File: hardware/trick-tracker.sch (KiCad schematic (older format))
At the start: 47 parts, among them J1 USB4105-GF-A, J2 S2B-PH-K, J3 QWiiC, U1 MS88SF2, U2 DPS368XTSA1, U3 LSM9DS1, U4 MCP73831-2-OT, U5 MIC5504-3.3YM5

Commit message: Add Micro SD-Card holder
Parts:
- removed LED1: APHF1608LSEEQBDZGKC, APHF1608LSEEQBDZGKC:APHF1608LSEEQBDZGKC, symbol APHF1608LSEEQBDZGKC:APHF1608LSEEQBDZGKC
- removed R8: 2k2, Resistor_SMD:R_0603_1608Metric, symbol Device:R_Small
- removed R9: 390R, Resistor_SMD:R_0603_1608Metric, symbol Device:R_Small
- added D4: GREEN, LED_SMD:LED_0603_1608Metric, symbol Device:LED_Small
- added H3, H4: MountingHole, MountingHole:MountingHole_2.5mm, symbol Mechanical:MountingHole
- added J4: MEM2051-00-195-00-A, MEM2051-00-195-00-A:GCT_MEM2051-00-195-00-A, symbol MEM2051-00-195-00-A:MEM2051-00-195-00-A
- R7: value 1k2 -> 470
- U4: value MCP73831-2-OT -> MCP73831/OT
- gave numbers to parts that had none: 3
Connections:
- net labels added: CS, MISO, MOSI, SCK, SD_DETECT
- net labels removed: CC1, CC2, LED_BLUE, LED_GREEN, LED_RED, NFC1
- wire segments 183 -> 185
- no-connect marks 8 -> 9
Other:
- moved on the sheet: C10, C11, C12, C5, C6, C7, C8, C9, D1, H1, H2, J1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

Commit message: Moved components
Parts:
- added D5: DSS13UTR, Diode_SMD:D_SOD-123F, symbol Device:D_Schottky
- D1: value MBR120 -> DSS13UTR; footprint Diode_SMD:D_0603_1608Metric -> Diode_SMD:D_SOD-123F
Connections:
- net VBUS: now also D5.2 (A); no longer C1.1, D1.1 (K), S3.3 (COM), U5.1 (VIN)
- new net VIN: C1.1, D1.1 (K), D5.1 (K), S3.3 (COM), U5.1 (VIN)
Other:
- moved on the sheet: D1
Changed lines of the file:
@@
 Text Label 7850 3700 0    50   ~ 0
 VBUS
-Text Label 7850 3950 0    50   ~ 0
+Text Label 7850 4050 0    50   ~ 0
 VBAT
 Wire Wire Line
@@
 	9100 3900 9100 3950
 Wire Wire Line
-	7850 3700 8550 3700
-Wire Wire Line
 	9100 3700 9400 3700
-Wire Wire Line
-	8550 3700 8550 3950
-Connection ~ 8550 3700
 Wire Wire Line
 	9700 4150 9400 4150
@@
 L Device:D_Schottky D1
 U 1 1 60B07CC4
-P 8300 3950
-F 0 "D1" H 8300 3733 50  0000 C CNN
-F 1 "MBR120" H 8300 3824 50  0000 C CNN
-F 2 "Diode_SMD:D_0603_1608Metric" H 8300 3950 50  0001 C CNN
-F 3 "~" H 8300 3950 50  0001 C CNN
-	1    8300 3950
+P 8300 4050
+F 0 "D1" H 8300 3833 50  0000 C CNN
+F 1 "DSS13UTR" H 8300 3924 50  0000 C CNN
+F 2 "Diode_SMD:D_SOD-123F" H 8300 4050 50  0001 C CNN
+F 3 "~" H 8300 4050 50  0001 C CNN
+	1    8300 4050
 	-1   0    0    1
 $EndComp
 Wire Wire Line
-	8450 3950 8550 3950
-Wire Wire Line
-	8150 3950 7850 3950
+	8450 4050 8550 4050
+Wire Wire Line
+	8150 4050 7850 4050
 $Comp
 L Connector:Conn_01x04_Male J3
@@
 Wire Wire Line
 	2750 2650 2250 2650
-Wire Wire Line
-	8550 3700 9100 3700
 $Comp
 L MEM2051-00-195-00-A:MEM2051-00-195-00-A J4
@@
 Wire Notes Line
 	500  5150 7350 5150
+$Comp
+L Device:D_Schottky D5
+U 1 1 60D58FCE
+P 8300 3700
+F 0 "D5" H 8300 3483 50  0000 C CNN
+F 1 "DSS13UTR" H 8300 3574 50  0000 C CNN
+F 2 "Diode_SMD:D_SOD-123F" H 8300 3700 50  0001 C CNN
+F 3 "~" H 8300 3700 50  0001 C CNN
+	1    8300 3700
+	-1   0    0    1
+$EndComp
+Wire Wire Line
+	7850 3700 8150 3700
+Wire Wire Line
+	8450 3700 8550 3700
+Wire Wire Line
+	8550 3700 8550 4050
+Connection ~ 8550 3700
+Wire Wire Line
+	8550 3700 9100 3700
 $EndSCHEMATC

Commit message: Changed LED resistor value to 1k
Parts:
- R5, R6: value 470 -> 1k
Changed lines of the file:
@@
 P 10500 2550
 F 0 "R5" V 10304 2550 50  0000 C CNN
-F 1 "470" V 10395 2550 50  0000 C CNN
+F 1 "1k" V 10395 2550 50  0000 C CNN
 F 2 "Resistor_SMD:R_0603_1608Metric" H 10500 2550 50  0001 C CNN
 F 3 "~" H 10500 2550 50  0001 C CNN
@@
 P 10500 2900
 F 0 "R6" V 10304 2900 50  0000 C CNN
-F 1 "470" V 10395 2900 50  0000 C CNN
+F 1 "1k" V 10395 2900 50  0000 C CNN
 F 2 "Resistor_SMD:R_0603_1608Metric" H 10500 2900 50  0001 C CNN
 F 3 "~" H 10500 2900 50  0001 C CNN

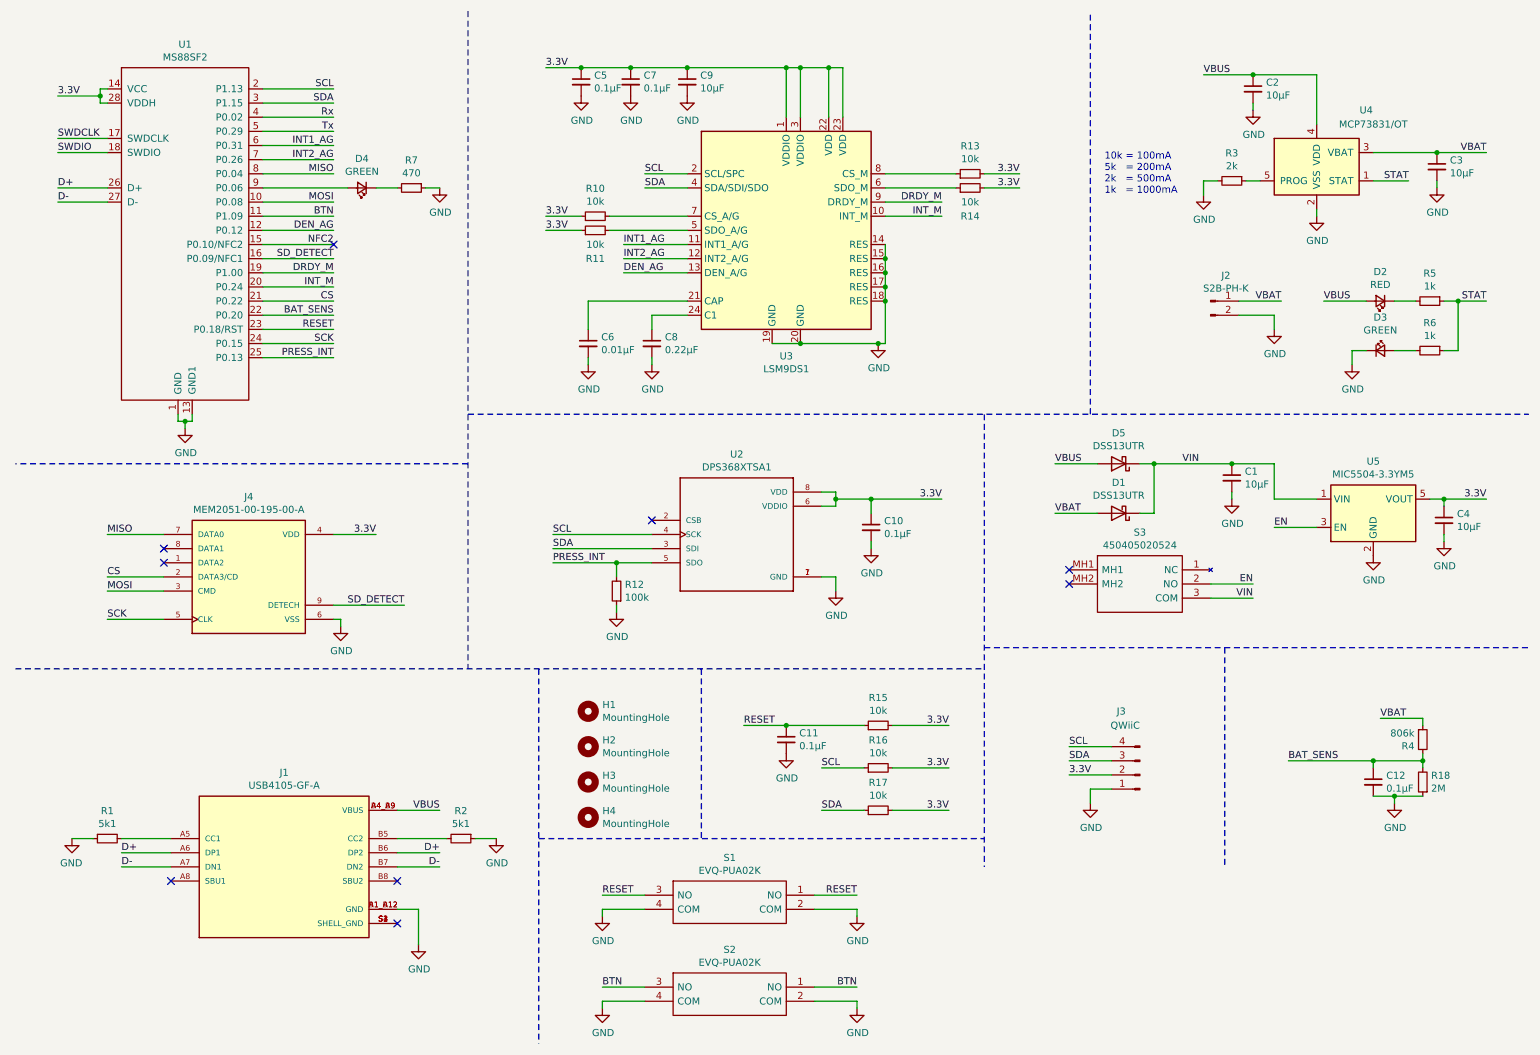
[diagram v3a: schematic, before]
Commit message: Add Labels to schematic
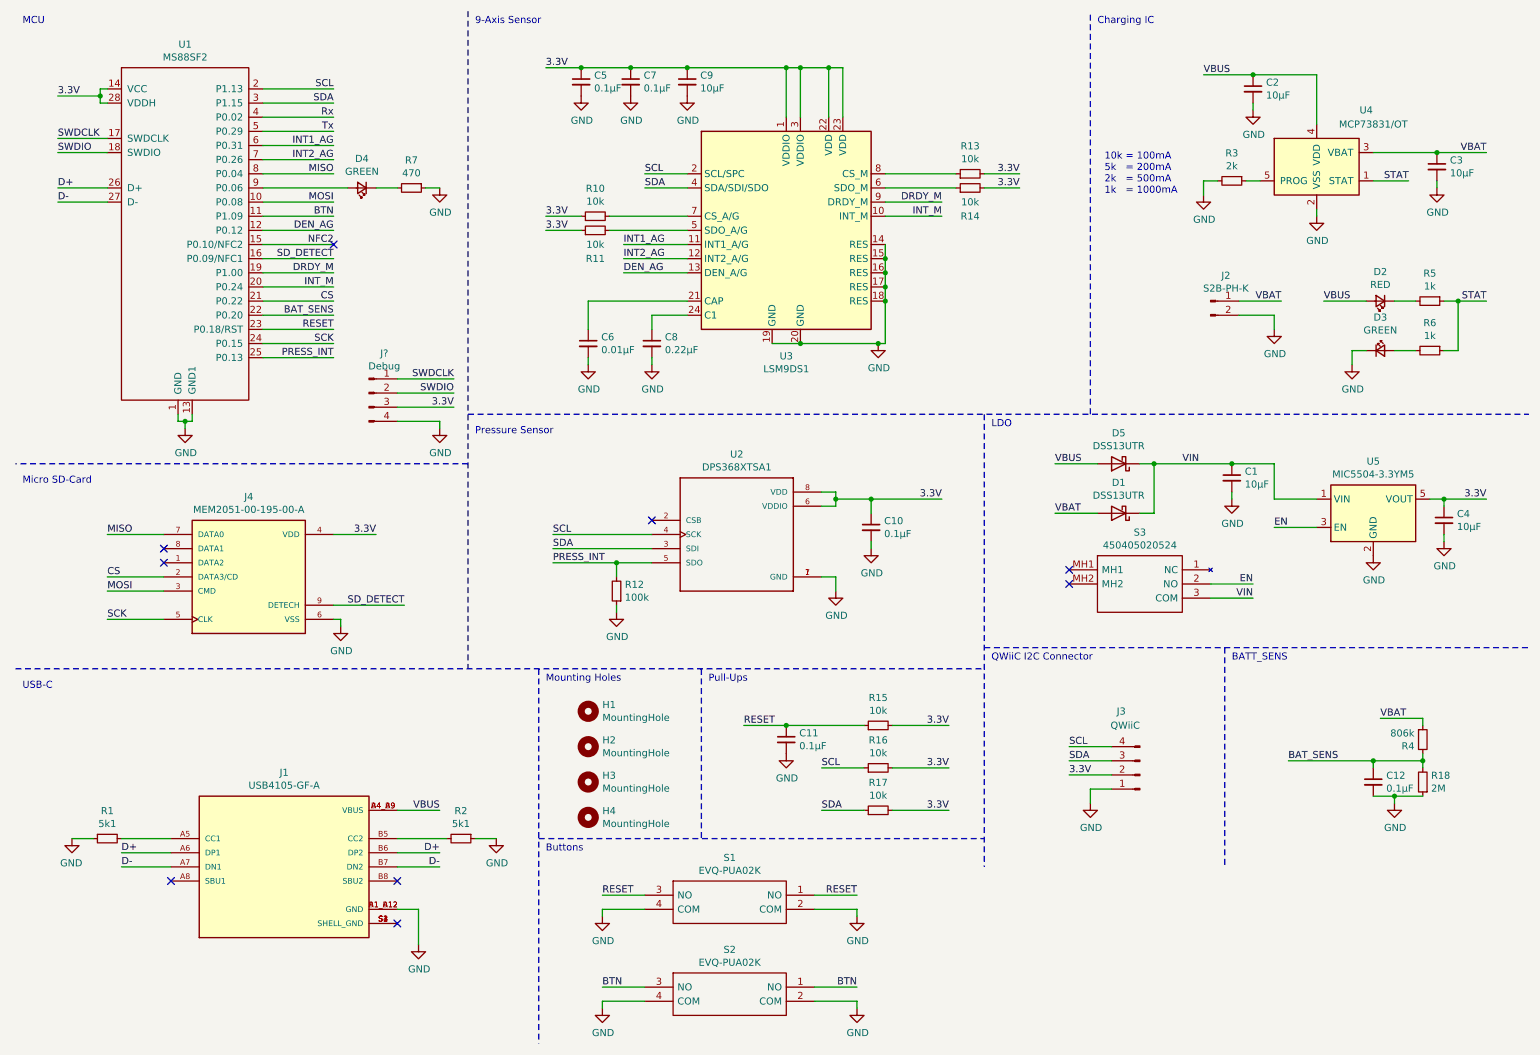
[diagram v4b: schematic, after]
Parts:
- added J?: Debug, symbol Connector:Conn_01x04_Male
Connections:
- net 3.3V: now also J?.3 (Pin_3)
- net GND: now also J?.4 (Pin_4)
- net SWDCLK: now also J?.1 (Pin_1)
- net SWDIO: now also J?.2 (Pin_2)
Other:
- note added: "9-Axis Sensor"
- note added: "BATT_SENS"
- note added: "Buttons"
- note added: "Charging IC"
- note added: "LDO"
- note added: "MCU"
- note added: "Micro SD-Card"
- note added: "Mounting Holes"
- note added: "Pressure Sensor"
- note added: "Pull-Ups"
- note added: "QWiiC I2C Connector"
- note added: "USB-C"
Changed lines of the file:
@@
 encoding utf-8
 Sheet 1 1
-Title ""
-Date ""
-Rev ""
+Title "Trick Tracker"
+Date "2021-05-23"
+Rev "v1.0"
 Comp ""
 Comment1 ""
@@
 Wire Wire Line
 	8550 3700 9100 3700
+Text Notes 9100 5100 0    50   ~ 0
+BATT_SENS
+Text Notes 7400 5100 0    50   ~ 0
+QWiiC I2C Connector
+Text Notes 7400 3450 0    50   ~ 0
+LDO
+Text Notes 8150 600  0    50   ~ 0
+Charging IC
+Text Notes 5400 5250 0    50   ~ 0
+Pull-Ups
+Text Notes 4250 5250 0    50   ~ 0
+Mounting Holes
+Text Notes 4250 6450 0    50   ~ 0
+Buttons
+Text Notes 550  5300 0    50   ~ 0
+USB-C
+Text Notes 550  3850 0    50   ~ 0
+Micro SD-Card
+Text Notes 3750 3500 0    50   ~ 0
+Pressure Sensor
+Text Notes 3750 600  0    50   ~ 0
+9-Axis Sensor
+Text Notes 550  600  0    50   ~ 0
+MCU
+$Comp
+L Connector:Conn_01x04_Male J?
+U 1 1 60AB9726
+P 3000 3200
+F 0 "J?" H 3108 3481 50  0000 C CNN
+F 1 "Debug" H 3108 3390 50  0000 C CNN
+F 2 "" H 3000 3200 50  0001 C CNN
+F 3 "~" H 3000 3200 50  0001 C CNN
+	1    3000 3200
+	1    0    0    -1
+$EndComp
+Text Label 3600 3100 2    50   ~ 0
+SWDCLK
+Text Label 3600 3200 2    50   ~ 0
+SWDIO
+$Comp
+L power:GND #PWR?
+U 1 1 60AB9E9C
+P 3500 3450
+F 0 "#PWR?" H 3500 3200 50  0001 C CNN
+F 1 "GND" H 3505 3277 50  0000 C CNN
+F 2 "" H 3500 3450 50  0001 C CNN
+F 3 "" H 3500 3450 50  0001 C CNN
+	1    3500 3450
+	1    0    0    -1
+$EndComp
+Text Label 3600 3300 2    50   ~ 0
+3.3V
+Wire Wire Line
+	3200 3100 3600 3100
+Wire Wire Line
+	3600 3200 3200 3200
+Wire Wire Line
+	3200 3300 3600 3300
+Wire Wire Line
+	3500 3450 3500 3400
+Wire Wire Line
+	3500 3400 3200 3400
 $EndSCHEMATC

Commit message: Exchanged battery connector with SMD version
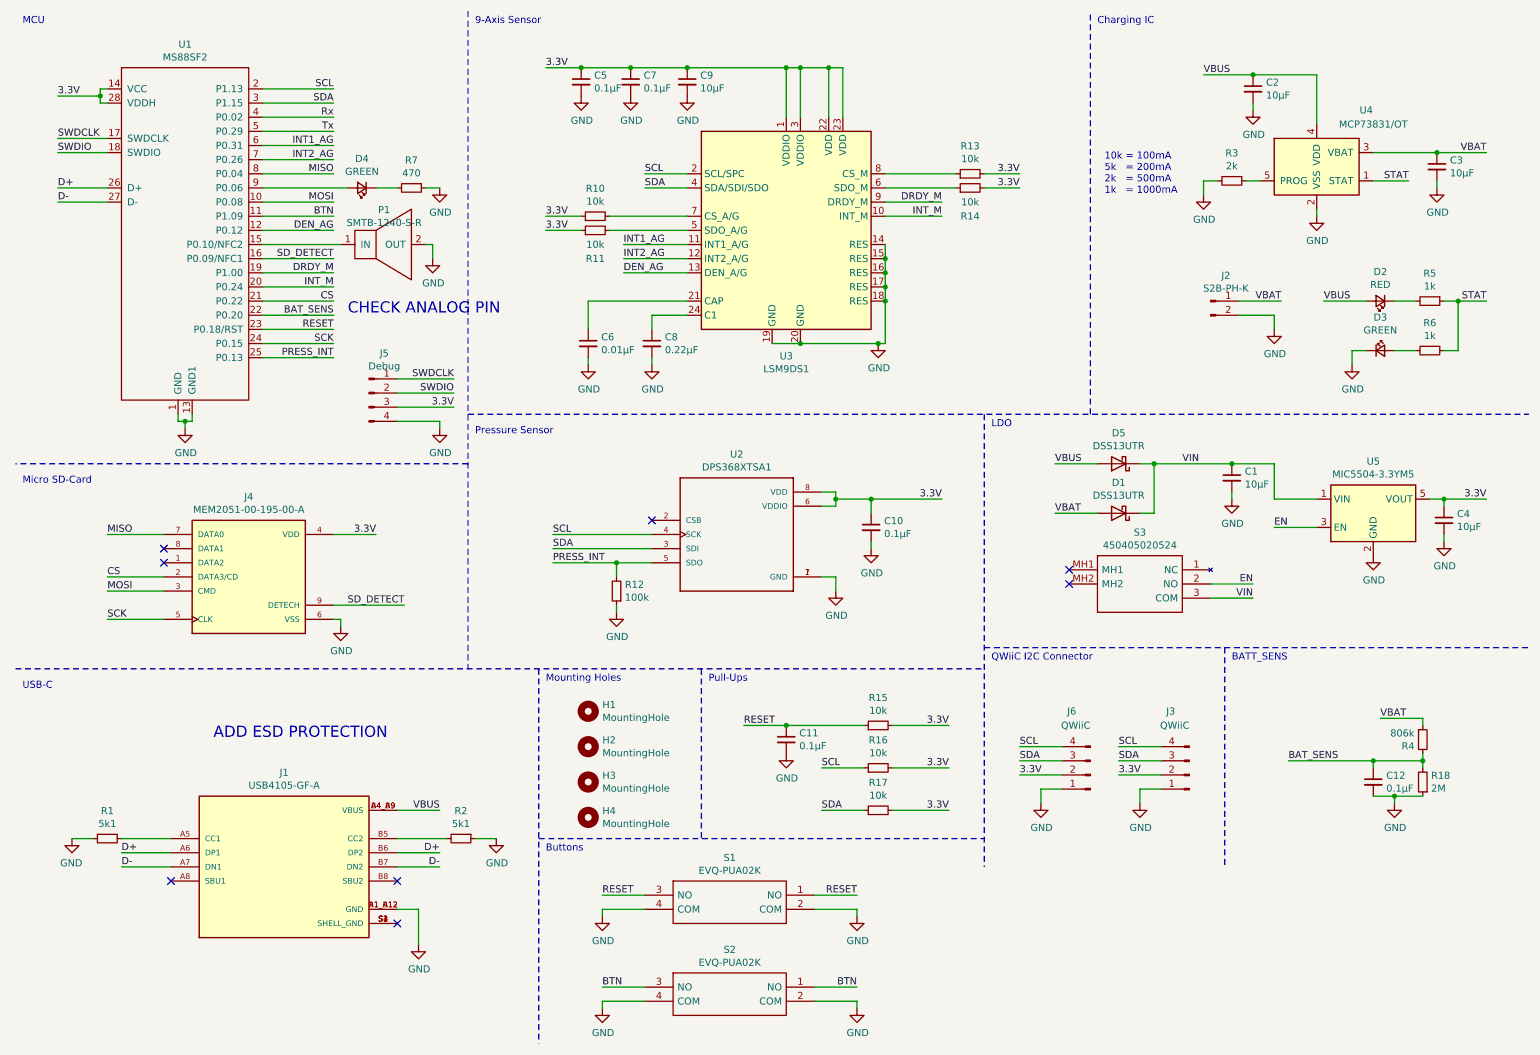
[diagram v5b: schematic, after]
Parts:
- added J6: QWiiC, Connector_JST:JST_SH_SM04B-SRSS-TB_1x04-1MP_P1.00mm_Horizontal, symbol Connector:Conn_01x04_Male
- added P1: SMTB-1240-S-R, SMTB-1240-S-R:SMTB-1240-S-R, symbol SMTB-1240-S-R:SMTB-1240-S-R
- J2: footprint Connector_JST:JST_PH_S2B-PH-K_1x02_P2.00mm_Horizontal -> Connector_JST:JST_PH_S2B-PH-SM4-TB_1x02-1MP_P2.00mm_Horizontal
- J5: renamed from J?; footprint (none) -> Connector_PinSocket_2.54mm:PinSocket_1x04_P2.54mm_Vertical
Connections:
- net 3.3V: now also J6.2 (Pin_2)
- net GND: now also J6.1 (Pin_1), P1.2 (OUT)
- net SCL: now also J6.4 (Pin_4)
- net SDA: now also J6.3 (Pin_3)
- net NFC2: no longer names the net of U1.15 (P0.10/NFC2)
- net NFC2: now also P1.1 (IN)
- no-connect marks 9 -> 8
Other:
- note added: "ADD ESD PROTECTION"
- note added: "CHECK ANALOG PIN"
- moved on the sheet: J3
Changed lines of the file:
@@
 F 0 "J2" H 9058 2731 50  0000 C CNN
 F 1 "S2B-PH-K" H 9058 2640 50  0000 C CNN
-F 2 "Connector_JST:JST_PH_S2B-PH-K_1x02_P2.00mm_Horizontal" H 8950 2550 50  0001 C CNN
+F 2 "Connector_JST:JST_PH_S2B-PH-SM4-TB_1x02-1MP_P2.00mm_Horizontal" H 8950 2550 50  0001 C CNN
 F 3 "~" H 8950 2550 50  0001 C CNN
 	1    8950 2550
@@
 L Connector:Conn_01x04_Male J3
 U 1 1 60B100CF
-P 8450 5900
-F 0 "J3" H 8550 5450 50  0000 L CNN
-F 1 "QWiiC" H 8450 5550 50  0000 L CNN
-F 2 "Connector_JST:JST_SH_SM04B-SRSS-TB_1x04-1MP_P1.00mm_Horizontal" H 8450 5900 50  0001 C CNN
-F 3 "~" H 8450 5900 50  0001 C CNN
-	1    8450 5900
+P 8800 5900
+F 0 "J3" H 8900 5450 50  0000 L CNN
+F 1 "QWiiC" H 8800 5550 50  0000 L CNN
+F 2 "Connector_JST:JST_SH_SM04B-SRSS-TB_1x04-1MP_P1.00mm_Horizontal" H 8800 5900 50  0001 C CNN
+F 3 "~" H 8800 5900 50  0001 C CNN
+	1    8800 5900
 	-1   0    0    1
 $EndComp
@@
 L power:GND #PWR0114
 U 1 1 60B105B9
-P 8100 6100
-F 0 "#PWR0114" H 8100 5850 50  0001 C CNN
-F 1 "GND" H 8105 5927 50  0000 C CNN
-F 2 "" H 8100 6100 50  0001 C CNN
-F 3 "" H 8100 6100 50  0001 C CNN
-	1    8100 6100
-	1    0    0    -1
-$EndComp
-Wire Wire Line
-	8250 6000 8100 6000
-Wire Wire Line
-	8100 6000 8100 6100
-Text Label 7950 5900 0    50   ~ 0
+P 8450 6100
+F 0 "#PWR0114" H 8450 5850 50  0001 C CNN
+F 1 "GND" H 8455 5927 50  0000 C CNN
+F 2 "" H 8450 6100 50  0001 C CNN
+F 3 "" H 8450 6100 50  0001 C CNN
+	1    8450 6100
+	1    0    0    -1
+$EndComp
+Wire Wire Line
+	8600 6000 8450 6000
+Wire Wire Line
+	8450 6000 8450 6100
+Text Label 8300 5900 0    50   ~ 0
 3.3V
-Text Label 7950 5800 0    50   ~ 0
+Text Label 8300 5800 0    50   ~ 0
 SDA
-Text Label 7950 5700 0    50   ~ 0
+Text Label 8300 5700 0    50   ~ 0
 SCL
 Wire Wire Line
-	7950 5900 8250 5900
-Wire Wire Line
-	7950 5800 8250 5800
-Wire Wire Line
-	7950 5700 8250 5700
+	8300 5900 8600 5900
+Wire Wire Line
+	8300 5800 8600 5800
+Wire Wire Line
+	8300 5700 8600 5700
 $Comp
 L Device:C_Small C10
@@
 Wire Wire Line
 	2750 2050 2250 2050
-Text Label 2750 2150 2    50   ~ 0
-NFC2
-Wire Wire Line
-	2750 2150 2250 2150
 Wire Wire Line
 	2250 2250 2750 2250
-NoConn ~ 2750 2150
 Text Label 2750 2750 2    50   ~ 0
 RESET
@@
 MCU
 $Comp
-L Connector:Conn_01x04_Male J?
+L Connector:Conn_01x04_Male J5
 U 1 1 60AB9726
 P 3000 3200
-F 0 "J?" H 3108 3481 50  0000 C CNN
+F 0 "J5" H 3108 3481 50  0000 C CNN
 F 1 "Debug" H 3108 3390 50  0000 C CNN
-F 2 "" H 3000 3200 50  0001 C CNN
+F 2 "Connector_PinSocket_2.54mm:PinSocket_1x04_P2.54mm_Vertical" H 3000 3200 50  0001 C CNN
 F 3 "~" H 3000 3200 50  0001 C CNN
 	1    3000 3200
@@
 SWDIO
 $Comp
-L power:GND #PWR?
+L power:GND #PWR0132
 U 1 1 60AB9E9C
 P 3500 3450
-F 0 "#PWR?" H 3500 3200 50  0001 C CNN
+F 0 "#PWR0132" H 3500 3200 50  0001 C CNN
 F 1 "GND" H 3505 3277 50  0000 C CNN
 F 2 "" H 3500 3450 50  0001 C CNN
@@
 Wire Wire Line
 	3500 3400 3200 3400
+Text Notes 2850 2650 0    79   ~ 0
+CHECK ANALOG PIN
+Text Notes 1900 5650 0    79   ~ 0
+ADD ESD PROTECTION
+$Comp
+L SMTB-1240-S-R:SMTB-1240-S-R P1
+U 1 1 60ACE7E7
+P 3100 2150
+F 0 "P1" H 3107 2395 50  0000 C CNN
+F 1 "SMTB-1240-S-R" H 3107 2304 50  0000 C CNN
+F 2 "SMTB-1240-S-R:SMTB-1240-S-R" H 3100 2150 50  0001 C CNN
+F 3 "" H 3100 2150 50  0001 C CNN
+	1    3100 2150
+	1    0    0    -1
+$EndComp
+Wire Wire Line
+	2800 2150 2250 2150
+$Comp
+L power:GND #PWR0133
+U 1 1 60AEDF28
+P 3450 2250
+F 0 "#PWR0133" H 3450 2000 50  0001 C CNN
+F 1 "GND" H 3455 2077 50  0000 C CNN
+F 2 "" H 3450 2250 50  0001 C CNN
+F 3 "" H 3450 2250 50  0001 C CNN
+	1    3450 2250
+	1    0    0    -1
+$EndComp
+Wire Wire Line
+	3400 2150 3450 2150
+Wire Wire Line
+	3450 2150 3450 2250
+$Comp
+L Connector:Conn_01x04_Male J6
+U 1 1 60B2CE75
+P 8100 5900
+F 0 "J6" H 8200 5450 50  0000 L CNN
+F 1 "QWiiC" H 8100 5550 50  0000 L CNN
+F 2 "Connector_JST:JST_SH_SM04B-SRSS-TB_1x04-1MP_P1.00mm_Horizontal" H 8100 5900 50  0001 C CNN
+F 3 "~" H 8100 5900 50  0001 C CNN
+	1    8100 5900
+	-1   0    0    1
+$EndComp
+$Comp
+L power:GND #PWR0134
+U 1 1 60B2CE7B
+P 7750 6100
+F 0 "#PWR0134" H 7750 5850 50  0001 C CNN
+F 1 "GND" H 7755 5927 50  0000 C CNN
+F 2 "" H 7750 6100 50  0001 C CNN
+F 3 "" H 7750 6100 50  0001 C CNN
+	1    7750 6100
+	1    0    0    -1
+$EndComp
+Wire Wire Line
+	7900 6000 7750 6000
+Wire Wire Line
+	7750 6000 7750 6100
+Text Label 7600 5900 0    50   ~ 0
+3.3V
+Text Label 7600 5800 0    50   ~ 0
+SDA
+Text Label 7600 5700 0    50   ~ 0
+SCL
+Wire Wire Line
+	7600 5900 7900 5900
+Wire Wire Line
+	7600 5800 7900 5800
+Wire Wire Line
+	7600 5700 7900 5700
 $EndSCHEMATC
